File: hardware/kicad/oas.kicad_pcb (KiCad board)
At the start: 2 copper layers, 120 x 103.5 mm, 69 parts, among them J1 Phoenix_MSTBA_2,5/3-G-5,08 (2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, J10 Native-USB recovery (DNP), J2 UART/Boot Recovery (DNP), J3 JST SM06B-GHS-TB (SEN66 conne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, J4 1x5 P1.27mm header (HLK-LD241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, J5 ESP32 row A (pins 1..15, ante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, J6 ESP32 row B (pins 16..30, USB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, J7 MIKROE mikroBUS pins 1..8 (AN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, J8 MIKROE mikroBUS pins 9..16 (P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, J9 JST SM04B-SRSS-TB (Qwiic / St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, Q1 AO3401A, SW1 C&K PTS645VK392LFS, U1 LM2596S-5.0, U2 TPS62933

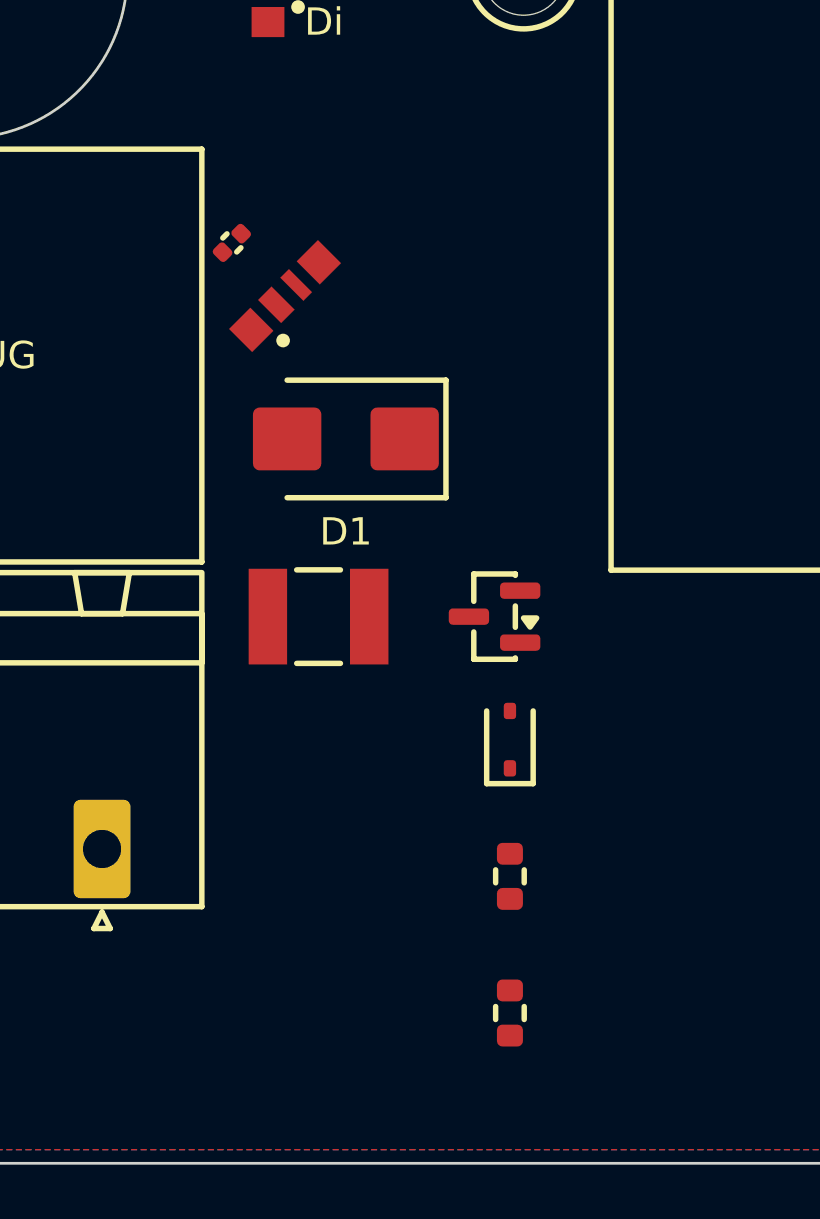
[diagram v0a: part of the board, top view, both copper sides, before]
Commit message: refactor(placement): protection cluster D1/F1/Q1 into the ZT1 column
v0.50 placement rework (task 2). D1, F1, Q1 were scattered across the
J1 corner (X 13-19, Y 17-23) forming a wall of F.Cu traces. They now
join D3/R4/R1 in one vertical column at X=+20, directly under ZT1:

  F1 +9.5 / Q1 +15.5 / D1 +22.5 / D3 +30 / R4 +35 / R1 +40  (all rot 90)

All six stack on the X=+20 axis so the reverse-polarity protection
chain routes as a near-straight run instead of a fan-out. D1's
designator moved F.SilkS -> F.Fab (east offset) -- no room for a silk
label in the packed column. D3/R4/R1 nudged +2 mm south for even pitch.

build.py 30/30 PASS, DRC 0, determinism 20/20.

Co-Authored-By: Claude Opus 4.7 (1M context) <noreply@anthropic.com>
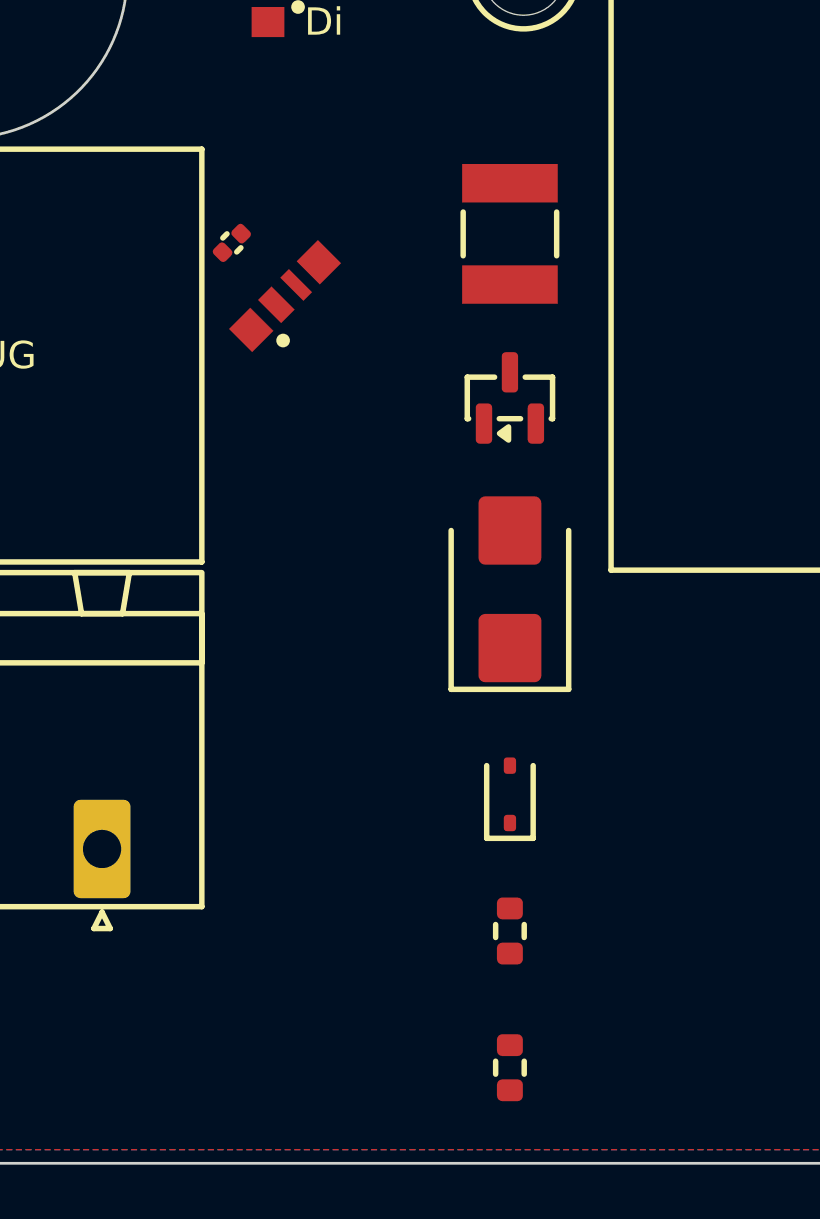
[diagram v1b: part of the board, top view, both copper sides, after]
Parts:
- moved F1 15.7 mm to (168.5, 114.5), turned to 90 degrees
- moved D1 8.14 mm to (168.5, 127.5), turned to 90 degrees
- moved Q1 8.02 mm to (168.5, 120.5), turned to 90 degrees
- moved D3 2.00 mm to (168.5, 135.0)
- moved R1 2.00 mm to (168.5, 145.0)
- moved R4 2.00 mm to (168.5, 140.0)
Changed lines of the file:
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@@
 (footprint "Diode_SMD:D_SMB"
 	(layer "F.Cu")
-	(at 162.5 122 180)
+	(at 168.5 127.5 90)
 (property "Reference" "D1"
-	(at 0 -3.1 180)
+	(at 0 -3.1 90)
 	(layer "F.SilkS")
 			(hide yes)
@@
 )
 (property "Value" "SMBJ24A"
-	(at 0 3.1 180)
+	(at 0 3.1 90)
 	(layer "F.Fab")
 			(hide yes)
@@
 		)
 	(pad "1" smd roundrect
-			(at -2.15 0 180)
+			(at -2.15 0 90)
 			(size 2.5 2.3)
 			(layers "F.Cu" "F.Mask" "F.Paste")
@@
 		)
 	(pad "2" smd roundrect
-			(at 2.15 0 180)
+			(at 2.15 0 90)
 			(size 2.5 2.3)
 			(layers "F.Cu" "F.Mask" "F.Paste")
@@
 (footprint "Package_TO_SOT_SMD:SOT-23"
 	(layer "F.Cu")
-	(at 167.938 128.5 180)
+	(at 168.5 120.5 90)
 (property "Reference" "Q1"
-	(at 0 -2.4 180)
+	(at 0 -2.4 90)
 	(layer "F.SilkS")
 			(hide yes)
@@
 )
 (property "Value" "AO3401A"
-	(at 0 2.4 180)
+	(at 0 2.4 90)
 	(layer "F.Fab")
 			(hide yes)
@@
 		)
 	(pad "1" smd roundrect
-			(at -0.9375 -0.95 180)
+			(at -0.9375 -0.95 90)
 			(size 1.475 0.6)
 			(layers "F.Cu" "F.Mask" "F.Paste")
@@
 		)
 	(pad "2" smd roundrect
-			(at -0.9375 0.95 180)
+			(at -0.9375 0.95 90)
 			(size 1.475 0.6)
 			(layers "F.Cu" "F.Mask" "F.Paste")
@@
 		)
 	(pad "3" smd roundrect
-			(at 0.9375 0 180)
+			(at 0.9375 0 90)
 			(size 1.475 0.6)
 			(layers "F.Cu" "F.Mask" "F.Paste")
@@
 (footprint "Diode_SMD:D_SOD-323"
 	(layer "F.Cu")
-	(at 168.5 133 90)
+	(at 168.5 135 90)
 (property "Reference" "D3"
 	(at 0 -1.5 90)
@@
         	(footprint "oas:Fuse_1812L_4532Metric"
         		(layer "F.Cu")
-        		(at 161.5 128.5 0)
+        		(at 168.5 114.5 90)
         		(descr "PTC polyfuse 750 mA hold / 1.5 A trip / 33 V (Littelfuse 1812L075/33DR, LCSC C151170, 1812 SMD).")
         		(attr smd)
         		(property "Reference" "F1"
-        			(at 0 -2.62 0)
+        			(at 0 -2.62 90)
         			(layer "F.SilkS")
 			(hide yes)
@@
         		)
         		(property "Value" "1812L075/33DR"
-        			(at 0 2.62 0)
+        			(at 0 2.62 90)
         			(layer "F.Fab")
         			(hide yes)
@@
         		)
         		(fp_text user "F1"
-        			(at 0 0 0)
+        			(at 0 0 90)
         			(layer "F.Fab")
         			(effects (font (size 1 1) (thickness 0.15)))
@@
         		)
 (pad "1" smd rect
-	(at -1.8534 0)
+	(at -1.8534 0 90)
 	(size 1.4067 3.4992)
 	(layers "F.Cu" "F.Mask" "F.Paste")
@@
 )
 (pad "2" smd rect
-	(at 1.8534 0)
+	(at 1.8534 0 90)
 	(size 1.4067 3.4992)
 	(layers "F.Cu" "F.Mask" "F.Paste")
@@
 (footprint "Resistor_SMD:R_0603_1608Metric"
 	(layer "F.Cu")
-	(at 168.5 138 90)
+	(at 168.5 140 90)
 (property "Reference" "R4"
 	(at 0 -1.45 90)
@@
 (footprint "Resistor_SMD:R_0603_1608Metric"
 	(layer "F.Cu")
-	(at 168.5 143 90)
+	(at 168.5 145 90)
 (property "Reference" "R1"
 	(at 0 -1.45 90)
@@
 )
 (gr_text "D1"
-	(at 162.5 125.4 0)
-	(layer "F.SilkS")
+	(at 172 127.5 0)
+	(layer "F.Fab")
 	(effects
-		(font (size 1 1) (thickness 0.2))
+		(font (size 1 1) (thickness 0.15))
 	)
 )
 (gr_text "F1"
-	(at 165.2 128.5 90)
+	(at 172.2 114.5 90)
 	(layer "F.Fab")
 	(effects
@@
 )
 (gr_text "Q1"
-	(at 167.938 131.5 0)
+	(at 168.5 123.5 0)
 	(layer "F.Fab")
 	(effects
@@
 )
 (gr_text "D3"
-	(at 170.8 133 0)
+	(at 170.8 135 0)
 	(layer "F.Fab")
 	(effects
@@
 )
 (gr_text "R4"
-	(at 170.8 138 0)
+	(at 170.8 140 0)
 	(layer "F.Fab")
 	(effects
@@
 )
 (gr_text "R1"
-	(at 170.8 143 0)
+	(at 170.8 145 0)
 	(layer "F.Fab")
 	(effects

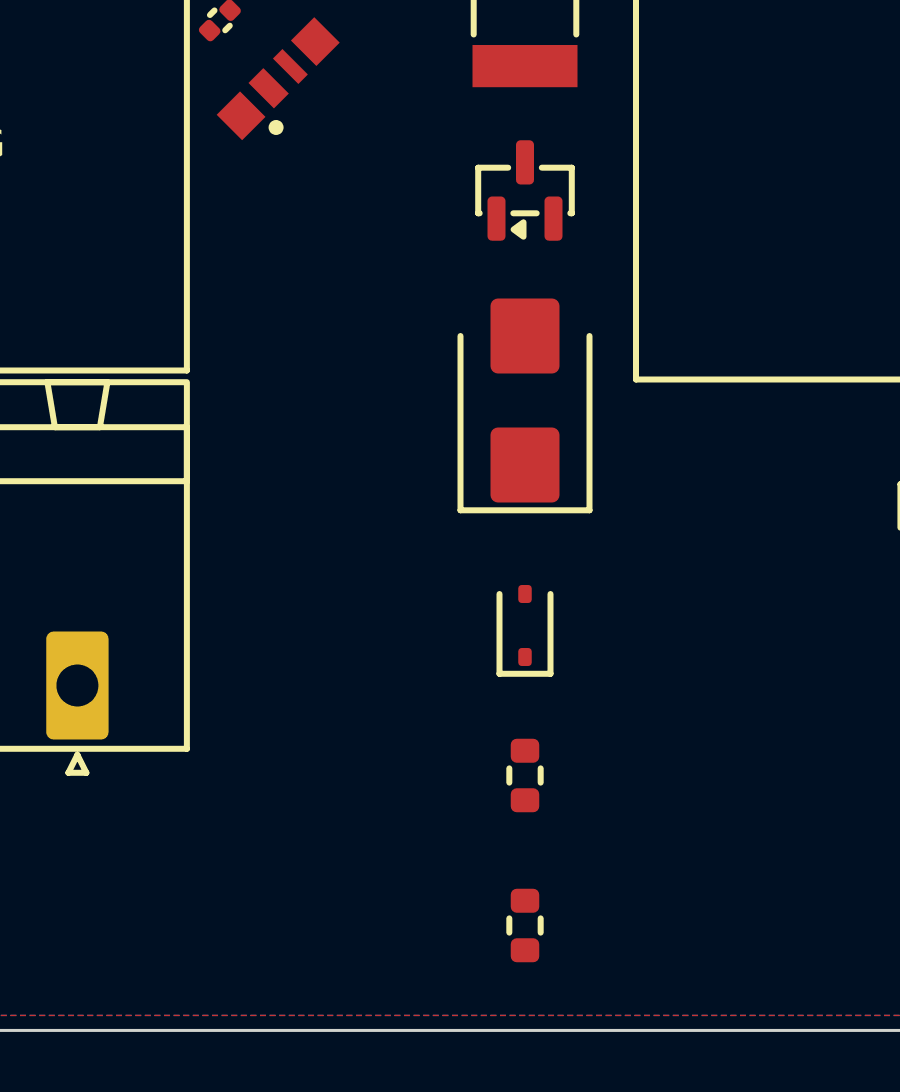
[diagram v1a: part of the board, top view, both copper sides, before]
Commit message: refactor(placement): split protection cluster into two columns
Per review: the single 6-tall column under ZT1 was too tall. Split into
two side-by-side vertical columns:

  right  X=+20  : F1 +9.5 / Q1 +15.5 / D1 +22.5   (in-line 24V devices)
  left   X=+15  : D3 +16.5 / R4 +21.5 / R1 +26.5   (Q1 gate network)

The left column was dropped ~5.5 mm south of its first try to clear the
SK6812 LED-ring footprint D12 at (+11.7, +11.7) (courtyards_overlap).
D3/R4/R1 designators flipped to the west (F.Fab) so they sit clear of
the right column.

build.py 30/30 PASS, DRC 0, determinism 20/20.

Co-Authored-By: Claude Opus 4.7 (1M context) <noreply@anthropic.com>
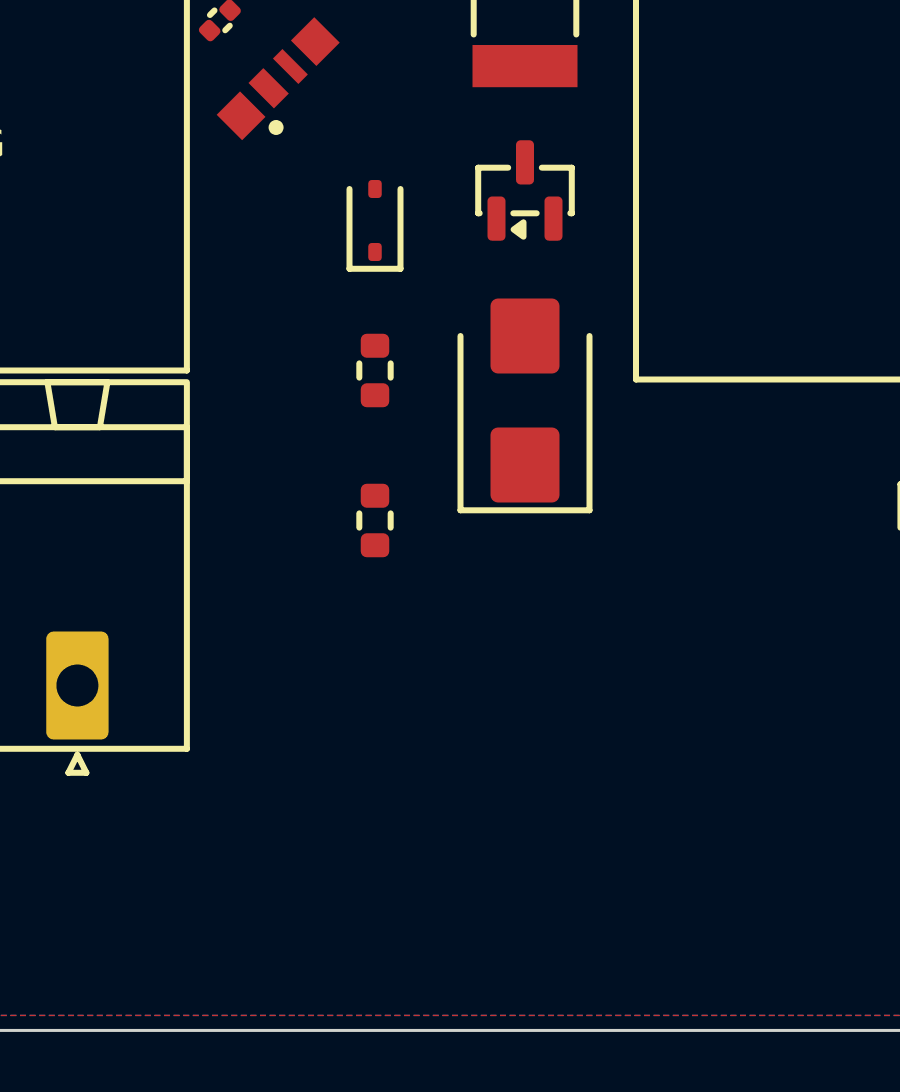
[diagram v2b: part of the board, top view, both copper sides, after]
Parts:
- moved D3 14.4 mm to (163.5, 121.5)
- moved R1 14.4 mm to (163.5, 131.5)
- moved R4 14.4 mm to (163.5, 126.5)
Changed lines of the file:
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@@
 (footprint "Diode_SMD:D_SOD-323"
 	(layer "F.Cu")
-	(at 168.5 135 90)
+	(at 163.5 121.5 90)
 (property "Reference" "D3"
 	(at 0 -1.5 90)
@@
 (footprint "Resistor_SMD:R_0603_1608Metric"
 	(layer "F.Cu")
-	(at 168.5 140 90)
+	(at 163.5 126.5 90)
 (property "Reference" "R4"
 	(at 0 -1.45 90)
@@
 (footprint "Resistor_SMD:R_0603_1608Metric"
 	(layer "F.Cu")
-	(at 168.5 145 90)
+	(at 163.5 131.5 90)
 (property "Reference" "R1"
 	(at 0 -1.45 90)
@@
 )
 (gr_text "D3"
-	(at 170.8 135 0)
+	(at 161 121.5 0)
 	(layer "F.Fab")
 	(effects
@@
 )
 (gr_text "R4"
-	(at 170.8 140 0)
+	(at 161 126.5 0)
 	(layer "F.Fab")
 	(effects
@@
 )
 (gr_text "R1"
-	(at 170.8 145 0)
+	(at 161 131.5 0)
 	(layer "F.Fab")
 	(effects
